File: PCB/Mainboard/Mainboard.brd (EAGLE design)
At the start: 60 x 150 mm, 61 parts, among them IC1 FT232RL, T1 BC847, T2 BC847

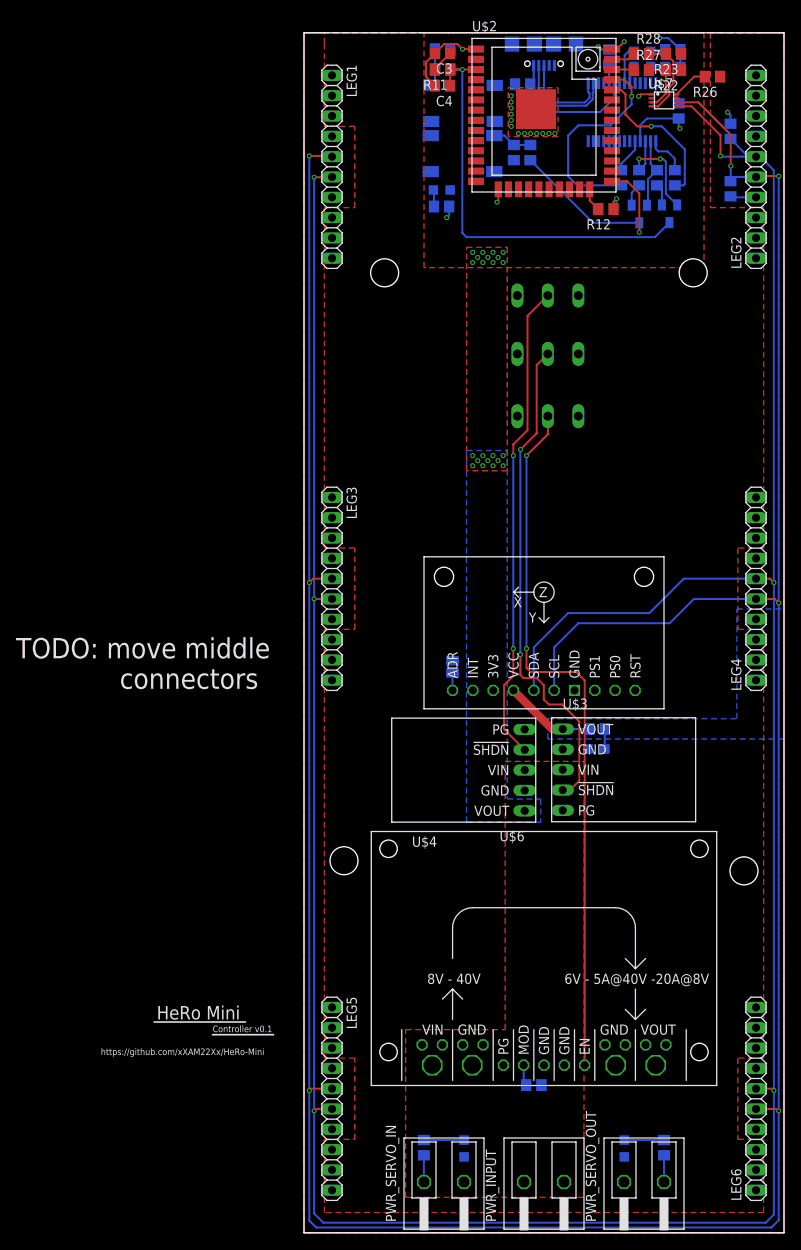
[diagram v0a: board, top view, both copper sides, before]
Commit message: finalised routing, added 3D-Models
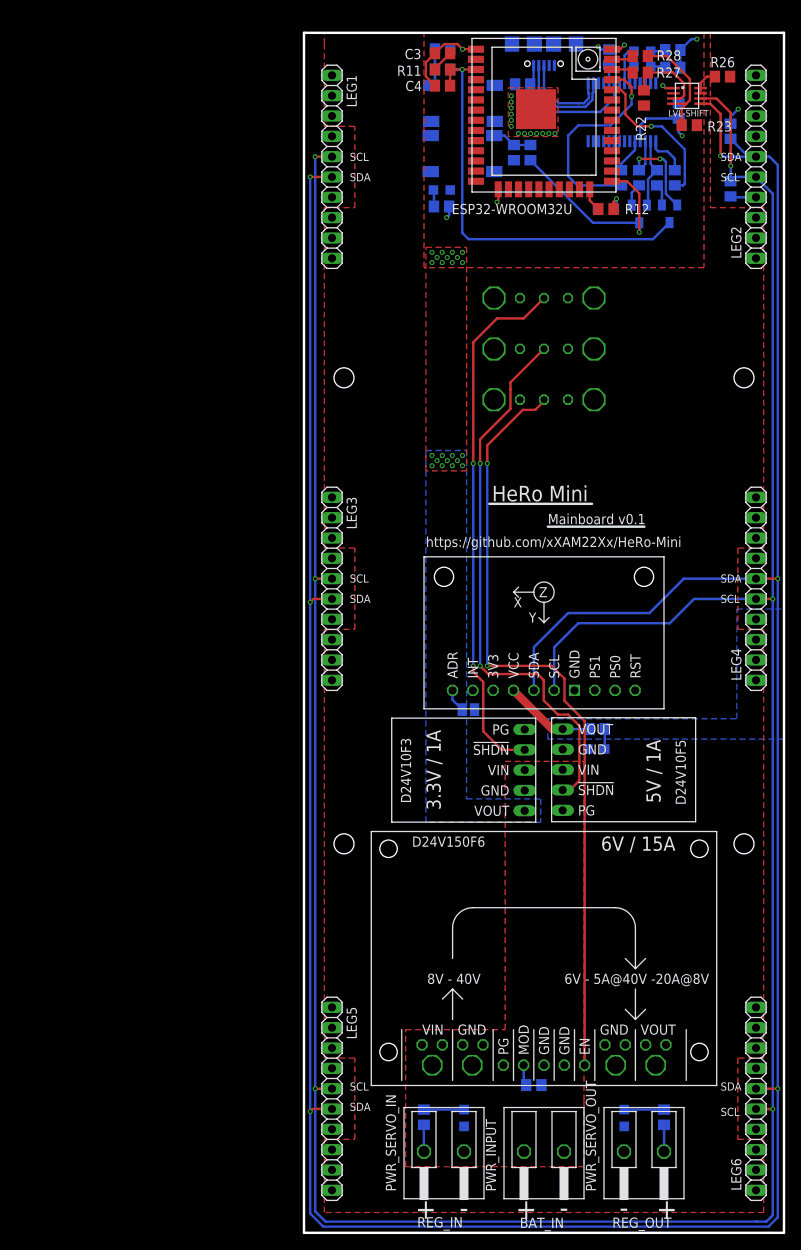
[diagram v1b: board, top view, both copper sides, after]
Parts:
- removed LED6, LED7: (no value), led:CHIP-LED0805
- removed S3, S4, S5: (no value), switch:255SB
- removed SJ1: (no value), jumper:SJ
- removed U$7: PCA9306, HeRo:PCA9306
- added 12V, 6V: (no value), led:CHIP-LED0805
- added ESP-PWR, LEG-PWR, SERVO-PWR: CSS-1202, HeRo:CSS-1202
- added IMU-ADDR: (no value), jumper:SJ
- added LVL-SHIFT: PCA9306, HeRo:PCA9306
- moved R23 9.13 mm to (48.2, 138.5)
- moved R22 5.07 mm to (42.5, 141.9), turned to 90 degrees
- moved PWR_INPUT 3.81 mm to (30.0, 10.2)
- moved PWR_SERVO_IN 3.81 mm to (17.5, 10.2)
- moved PWR_SERVO_OUT 3.81 mm to (42.5, 10.2)
- moved R17 3.81 mm to (45.0, 14.5)
- moved R18 3.81 mm to (15.0, 14.5)
- moved R26 1.27 mm to (52.3, 144.5)
- moved R27 0.33 mm to (42.0, 145.0)
- moved R28 0.31 mm to (42.0, 147.1)
- renumbered IC1 to FTDI, LED1 to TX, LED2 to RX, LED3 to ESP, LED4 to 3.3V, LED5 to 5V, U$2 to ESP32-WROOM32U, U$3 to D24V10F5, U$4 to D24V150F6, U$5 to 9-AXIS-IMU, U$6 to D24V10F3, U$8 to EN, U$9 to IO0
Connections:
- net +3V3: now also LVL-SHIFT.VREF1; no longer U$7.VREF1
- net EN_3V3: now also ESP-PWR.P; no longer S5.2
- net EN_5V: now also LEG-PWR.P; no longer S4.2
- net EN_SERVO: now also SERVO-PWR.P; no longer S3.2
- net GND: now also 12V.C, 6V.C, ESP-PWR.S, IMU-ADDR.2, LEG-PWR.S, LVL-SHIFT.GND, SERVO-PWR.S; no longer LED6.C, LED7.C, S3.3, S4.3, S5.3, SJ1.2, U$7.GND
- net IMU_ADR: now also IMU-ADDR.1; no longer SJ1.1
- net N$16: now also 6V.A; no longer LED6.A
- net N$18: now also 12V.A; no longer LED7.A
- net N$23: now also LVL-SHIFT.EN, LVL-SHIFT.VREF2; no longer U$7.EN, U$7.VREF2
- net SCL_3V3: now also LVL-SHIFT.SCL1; no longer U$7.SCL1
- net SCL_5V: now also LVL-SHIFT.SCL2; no longer U$7.SCL2
- net SDA_3V3: now also LVL-SHIFT.SDA1; no longer U$7.SDA1
- net SDA_5V: now also LVL-SHIFT.SDA2; no longer U$7.SDA2
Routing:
- net SCL_5V: track 391.5 -> 380.6 mm, vias 7 -> 6
- net EN_SERVO: track 88.6 -> 96.8 mm
- net EN_5V: track 62.3 -> 69.3 mm
- net EN_3V3: track 60.1 -> 66.4 mm
- net SDA_3V3: track 10.7 -> 14.2 mm
- net SDA_5V: track 387.8 -> 391.3 mm
- net SCL_3V3: track 7.27 -> 10.5 mm
- net N$23: track 4.97 -> 3.42 mm
- net IMU_ADR: track 2.18 -> 2.90 mm
- net +5V: track 16.3 -> 17.0 mm
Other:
- board text added: "+"
- board text added: "-"
- board text added: "3.3V / 1A"
- board text added: "5V / 1A"
- board text added: "6V / 15A"
- board text added: "BAT_IN"
- board text added: "EN"
- board text added: "IO0"
- board text added: "Mainboard v0.1"
- board text added: "REG_IN"
- board text added: "REG_OUT"
- board text added: "SCL"
- board text added: "SDA"
- board text removed: "Controller v0.1"
- board text removed: "TODO: move middle connectors"
